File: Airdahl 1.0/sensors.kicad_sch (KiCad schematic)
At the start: 4 parts, among them J6 PRT-16766, U3 ADXL345, U4 BNO085, U5 BMP581

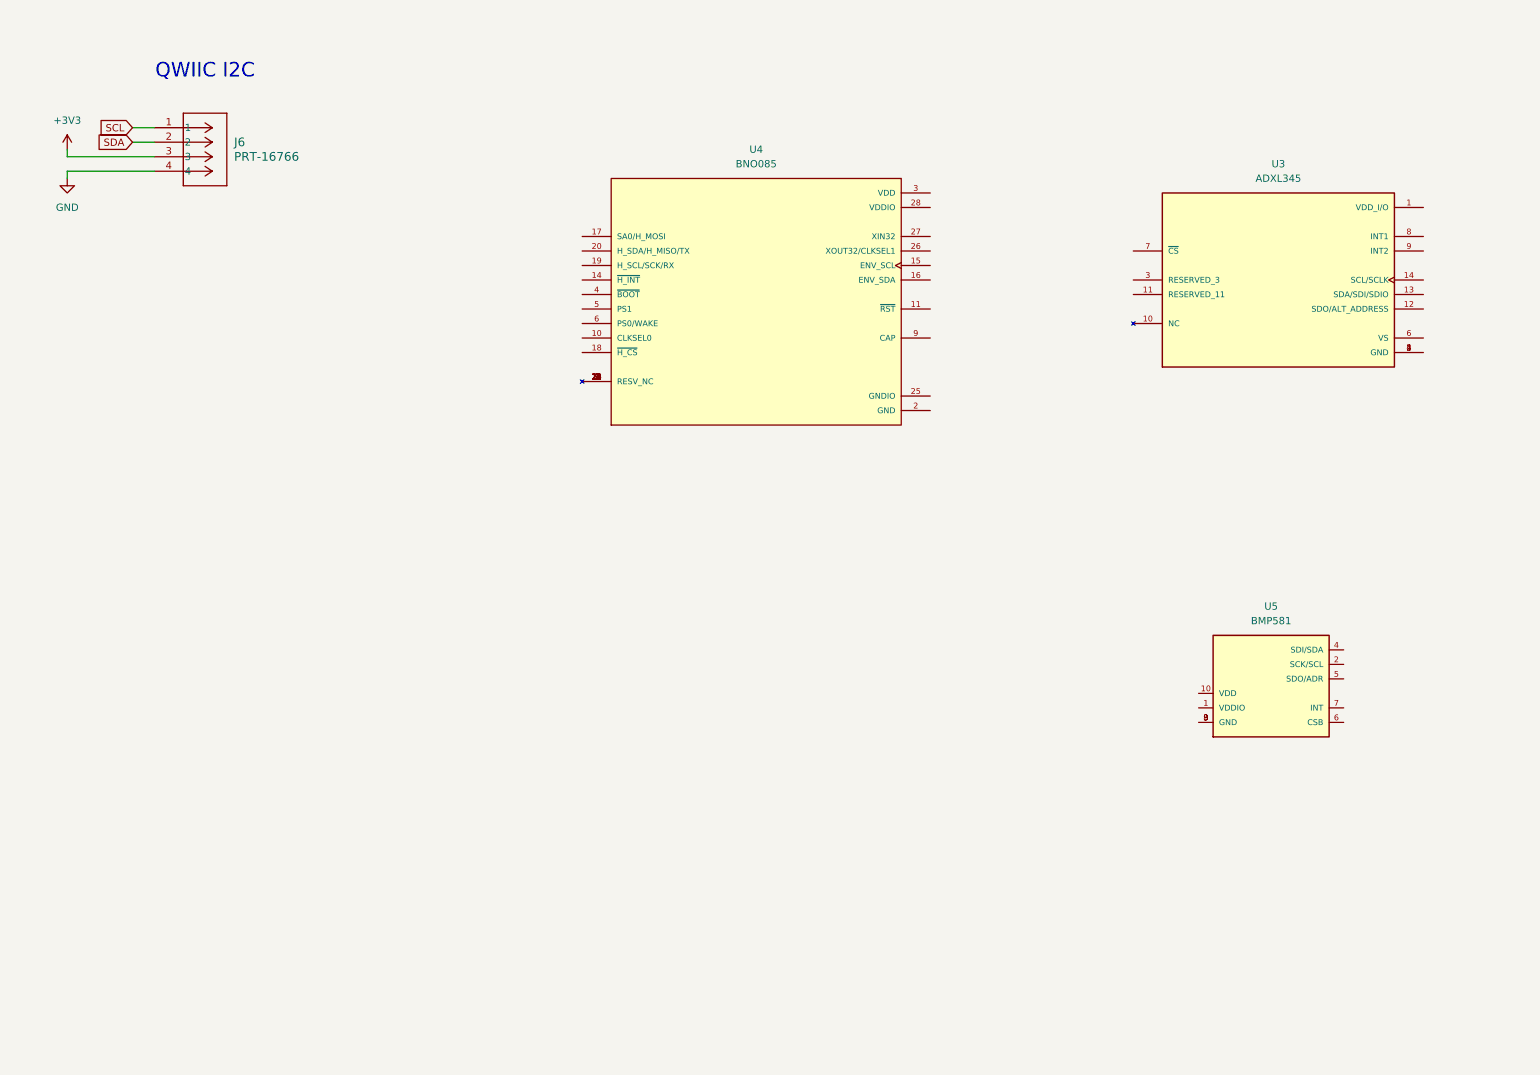
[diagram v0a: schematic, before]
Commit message: wired up dat ho (sitting on int/rst signals until we figure out rest of gpio)
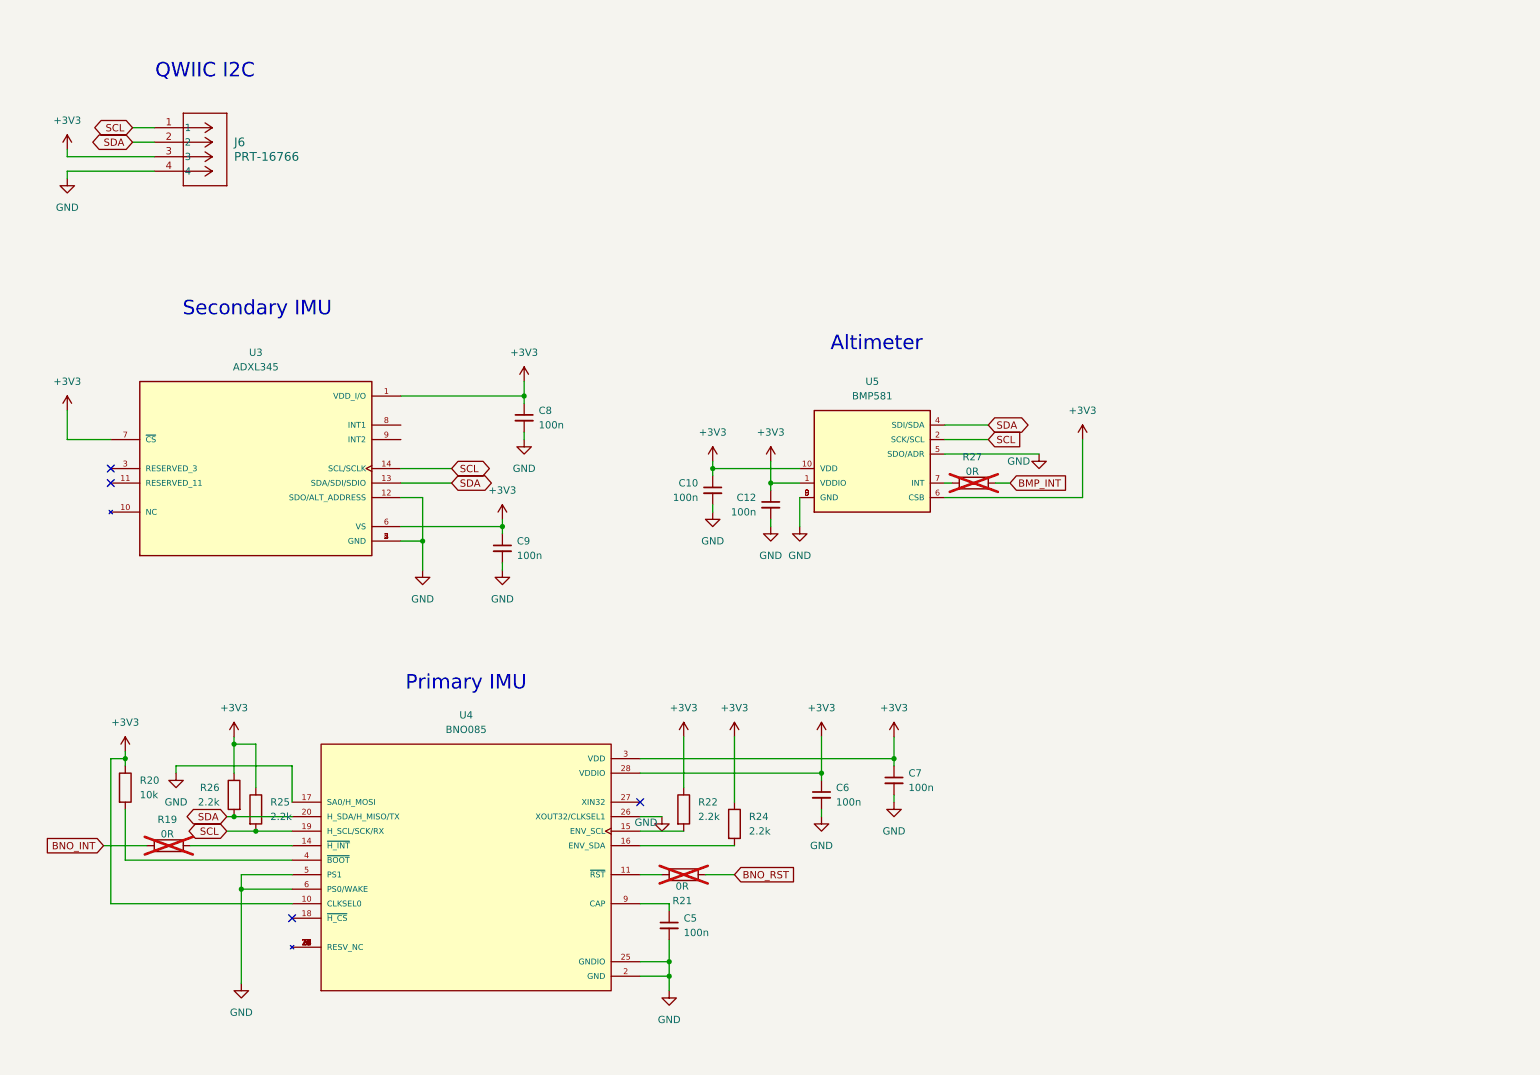
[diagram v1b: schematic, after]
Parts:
- added C10, C12, C5, C6, C7, C8, C9: 100n, Capacitor_SMD:C_0603_1608Metric_Pad1.08x0.95mm_HandSolder, symbol Device:C_Small
- added R19, R21, R27: 0R, Resistor_SMD:R_0603_1608Metric_Pad0.98x0.95mm_HandSolder, symbol Device:R
- added R20: 10k, Resistor_SMD:R_0603_1608Metric_Pad0.98x0.95mm_HandSolder, symbol Device:R
- added R22, R24, R25, R26: 2.2k, Resistor_SMD:R_0603_1608Metric_Pad0.98x0.95mm_HandSolder, symbol Device:R
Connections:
- net +3V3: now also U3.1 (VDD_I/O), U3.6 (VS), U3.7 (~{CS}), U4.10 (CLKSEL0), U4.28 (VDDIO), U4.3 (VDD), U5.1 (VDDIO), U5.10 (VDD), U5.6 (CSB), C10.1, C12.1, C6.1, C7.1, C8.1, C9.1, R20.1, R22.1, R24.1, R25.1, R26.1
- net GND: now also U3.12 (SDO/ALT_ADDRESS), U3.2 (GND), U3.4 (GND), U3.5 (GND), U4.17 (SA0/H_MOSI), U4.2 (GND), U4.25 (GNDIO), U4.26 (XOUT32/CLKSEL1), U4.5 (PS1), U4.6 (PS0/WAKE), U5.3 (GND), U5.5 (SDO/ADR), U5.8 (GND), U5.9 (GND), C10.2, C12.2, C5.2, C6.2, C7.2, C8.2, C9.2
- net SCL: now also U3.14 (SCL/SCLK), U4.19 (H_SCL/SCK/RX), U5.2 (SCK/SCL), R25.2
- net SDA: now also U3.13 (SDA/SDI/SDIO), U4.20 (H_SDA/H_MISO/TX), U5.4 (SDI/SDA), R26.2
- net at U5.7 (INT): now also R27.1
- net at U4.11 (~{RST}): now also R21.1
- net at U4.14 (~{H_INT}): now also R19.2
- net at U4.15 (ENV_SCL): now also R22.2
- net at U4.16 (ENV_SDA): now also R24.2
- net at U4.4 (~{BOOT}): now also R20.2
- net at U4.9 (CAP): now also C5.1
- new net BMP_INT: R27.2
- new net BNO_INT: R19.1
- new net BNO_RST: R21.2
- no-connect marks 0 -> 4
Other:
- note added: "Altimeter"
- note added: "Primary IMU"
- note added: "Secondary IMU"
- moved on the sheet: U3, U4, U5

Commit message: rfm wiring
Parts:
- added C13: 10n, Capacitor_SMD:C_0603_1608Metric_Pad1.08x0.95mm_HandSolder, symbol Device:C_Small
- added J7: CONUFL001-SMD-T, CONUFL001-SMD-T:LINX_CONUFL001-SMD-T, symbol CONUFL001-SMD-T:CONUFL001-SMD-T
- added U6: RFM95W-915S2, RFM95W-915S2:XCVR_RFM95W-915S2, symbol RFM95W-915S2:RFM95W-915S2
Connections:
- net +3V3: now also C13.1, U6.13 (3.3V)
- net GND: now also C13.2, J7.2, J7.3, U6.1 (GND), U6.10 (GND), U6.8 (GND)
- new net: J7.1, U6.9 (ANT)
- new net CS_RFM: U6.5 (NSS)
- new net D0_RFM: U6.14 (DIO0)
- new net MISO: U6.2 (MISO)
- new net MOSI: U6.3 (MOSI)
- new net RST_RFM: U6.6 (RESET)
- new net SCLK: U6.4 (SCK)
- no-connect marks 4 -> 9
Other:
- note added: "Telemetry"
- moved on the sheet: C10, C12, R27, U5

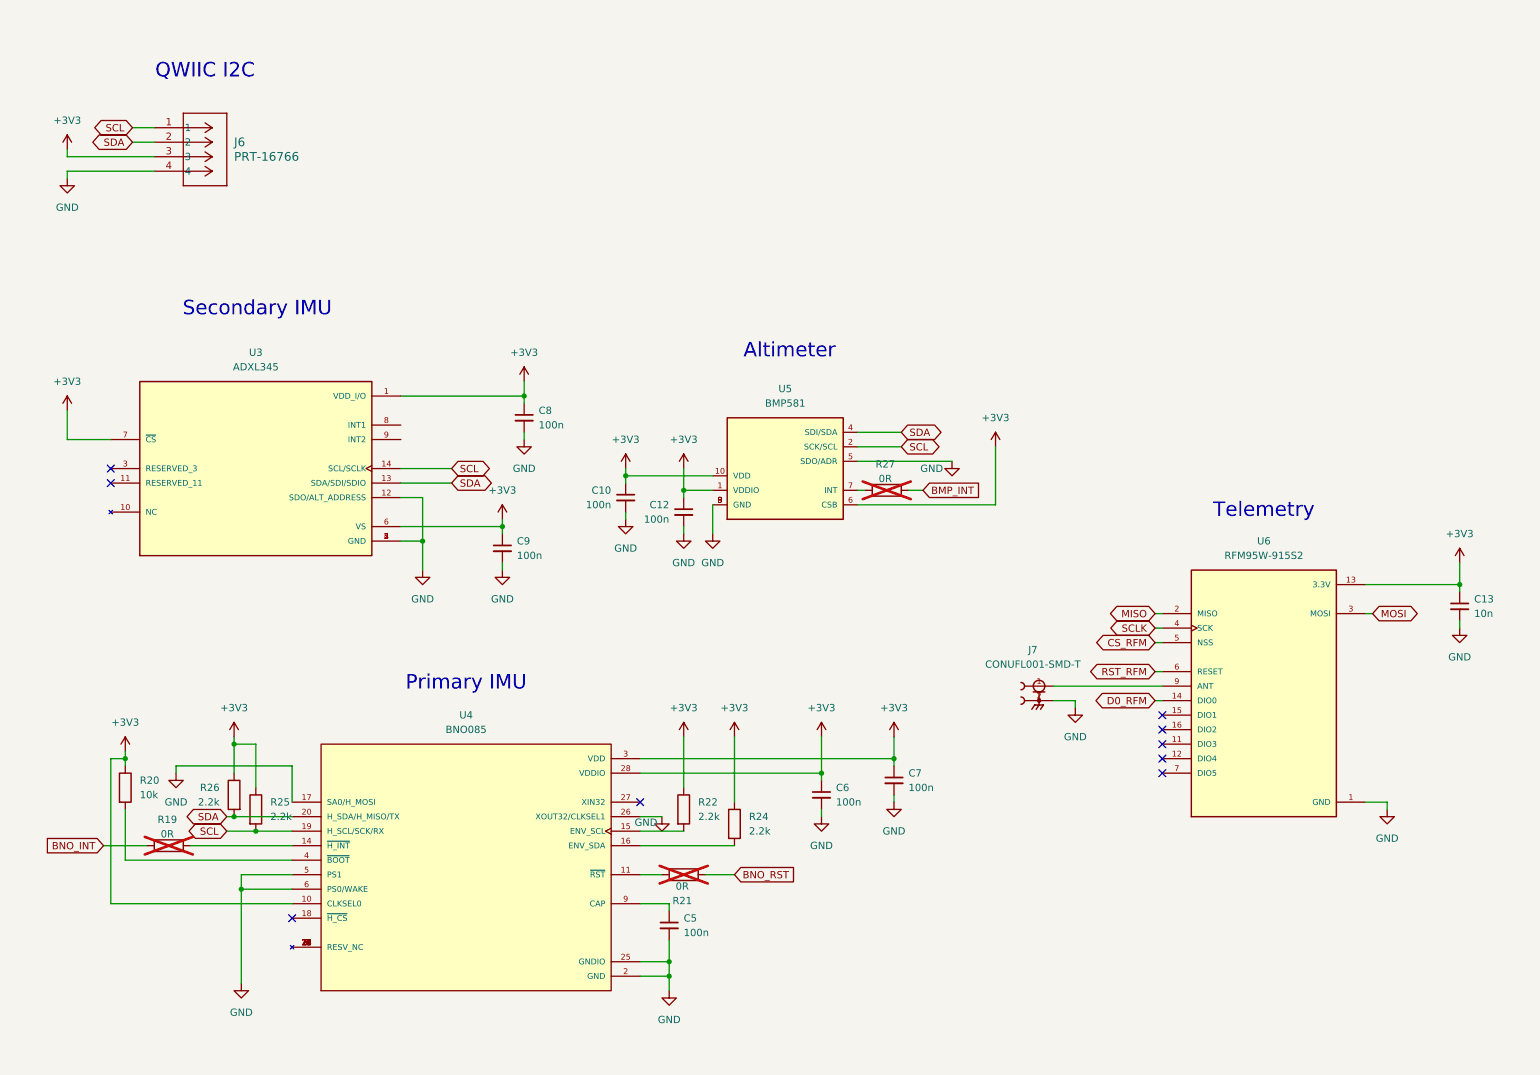
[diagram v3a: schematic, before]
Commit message: added 3.3V LDO, SD Card, spi breakout
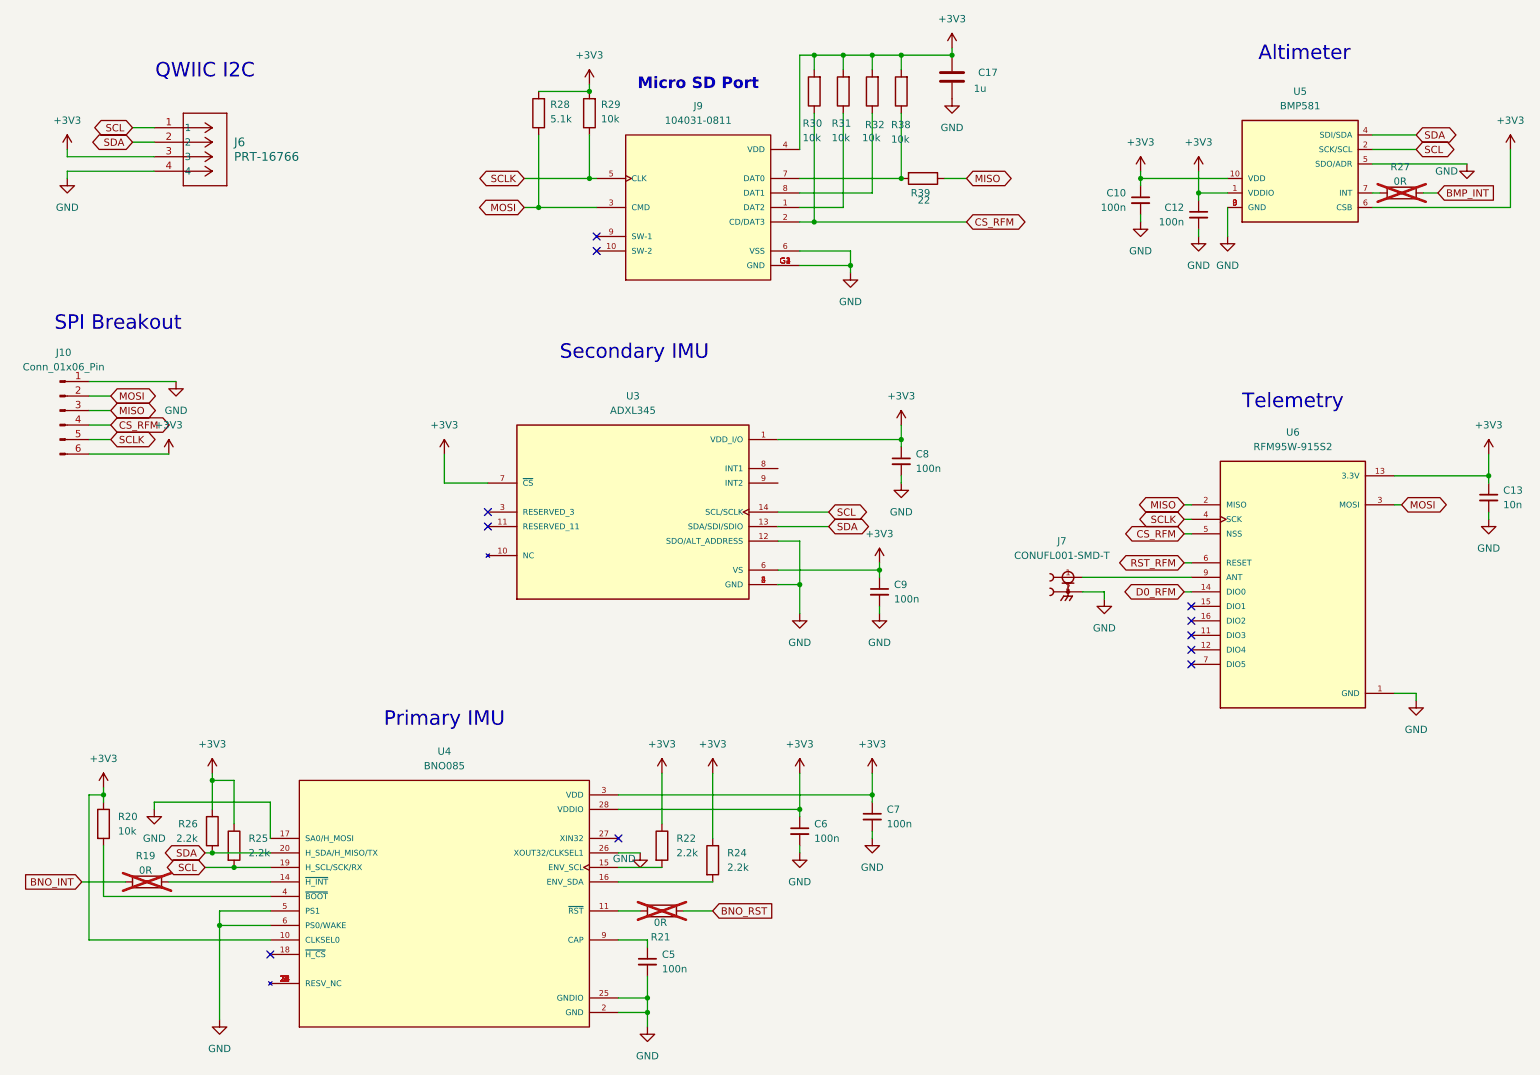
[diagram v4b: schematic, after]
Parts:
- added C17: 1u, Capacitor_SMD:C_0402_1005Metric, symbol Device:C
- added J10: Conn_01x06_Pin, Connector_PinSocket_2.54mm:PinSocket_1x06_P2.54mm_Vertical, symbol Connector:Conn_01x06_Pin
- added J9: 104031-0811, 104031-0811:MOLEX_104031-0811, symbol 104031-0811:104031-0811
- added R28: 5.1k, Resistor_SMD:R_0402_1005Metric, symbol Device:R
- added R29, R30, R31, R32, R38: 10k, Resistor_SMD:R_0402_1005Metric, symbol Device:R
- added R39: 22, Resistor_SMD:R_0402_1005Metric, symbol Device:R
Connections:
- net +3V3: now also C17.1, J10.6 (Pin_6), J9.4 (VDD), R28.2, R29.2, R30.2, R31.2, R32.2, R38.2
- net CS_RFM: now also J10.4 (Pin_4), J9.2 (CD/DAT3), R30.1
- net GND: now also C17.2, J10.1 (Pin_1), J9.6 (VSS), J9.G1 (GND), J9.G2 (GND), J9.G3 (GND), J9.G4 (GND)
- net MISO: now also J10.3 (Pin_3), R39.1
- net MOSI: now also J10.2 (Pin_2), J9.3 (CMD), R28.1
- net SCLK: now also J10.5 (Pin_5), J9.5 (CLK), R29.1
- new net: J9.7 (DAT0), R38.1, R39.2
- new net: J9.1 (DAT2), R31.1
- new net: J9.8 (DAT1), R32.1
- no-connect marks 9 -> 11
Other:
- note added: "Micro SD Port"
- note added: "SPI Breakout"
- moved on the sheet: C10, C12, C13, C5, C6, C7, C8, C9, J7, R19, R20, R21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

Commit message: added 5v buck, h bridge IC, updated jtag connections
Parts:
- U6: DESCRIPTION RFM95W LoRA Transceiver Module 915MHz -> (none)
